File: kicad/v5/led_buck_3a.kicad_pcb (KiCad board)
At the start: 2 copper layers, 44 x 44 mm, 28 parts, among them J1 LED+, J2 LED-, J3 JST_B3B-PH-SM4-TB(LF)(SN), J4 Conn_01x05, Q1 BSC022N04LSATMA, U1 MAX16820ATT, U2 ATtiny1616-M

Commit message: save
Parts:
- added TP1: TestPoint, TestPoint:TestPoint_Pad_1.0x1.0mm, F.Cu at (50.0, 63.8)
- added TP4: TestPoint, TestPoint:TestPoint_Pad_1.0x1.0mm, F.Cu at (48.0, 63.8)
- C1: footprint Capacitor_SMD:C_1210_3225Metric -> Capacitor_SMD:C_0805_2012Metric
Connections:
- U2 pad 15: unconnected-(U2-Pad15) -> Net-(U2-Pad15)
- U2 pad 16: unconnected-(U2-Pad16) -> Net-(U2-Pad16)
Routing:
- net Net-(U2-Pad15): track 0.00 -> 3.03 mm
- net Net-(U2-Pad16): track 0.00 -> 2.82 mm

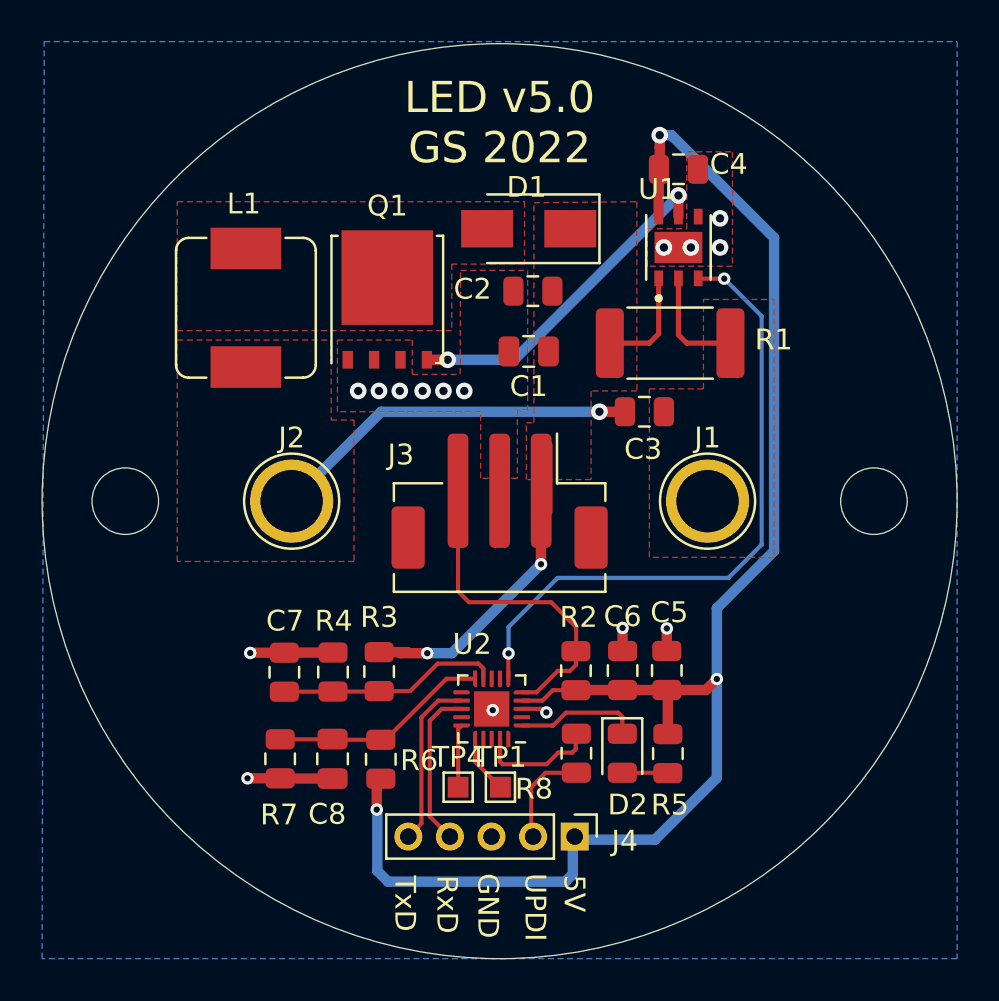
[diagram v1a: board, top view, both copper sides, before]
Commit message: - Neues PCB V5.1 - Ädernungen an den Akkufach 3D Teilen - Firmware überarbeitet
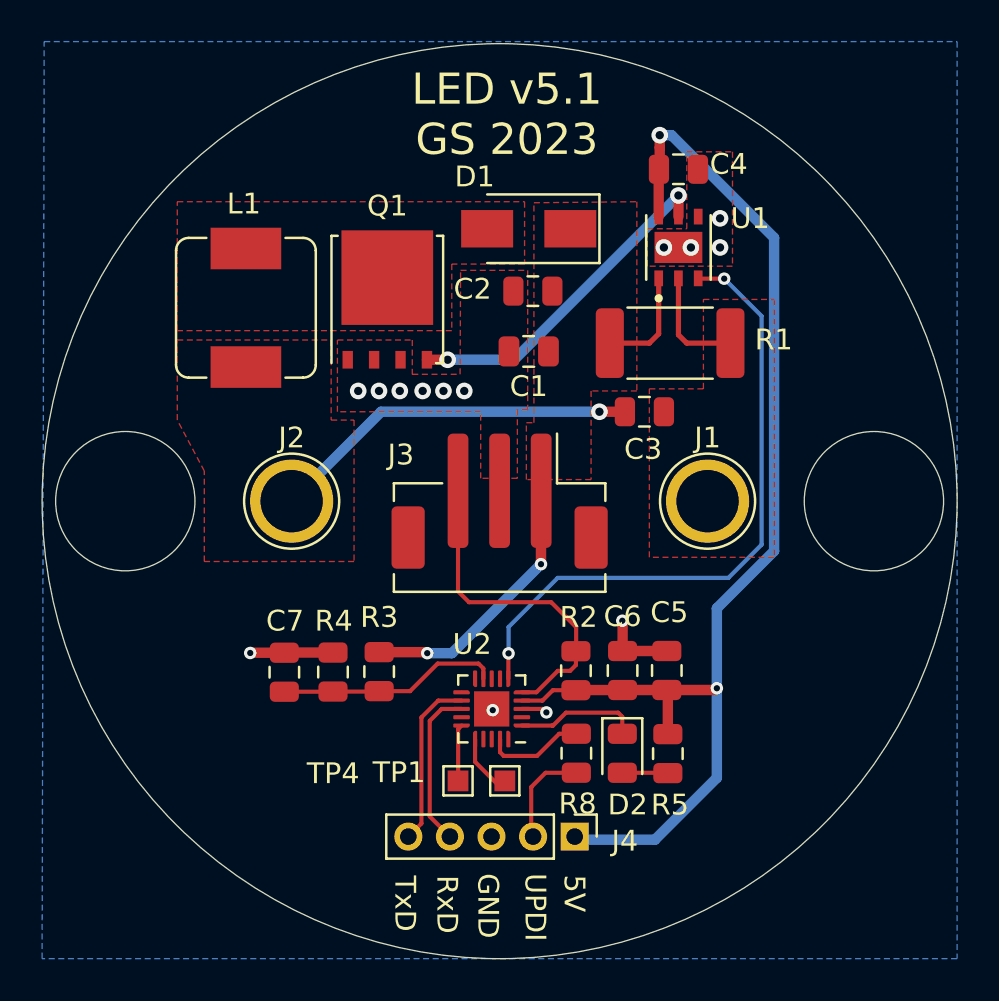
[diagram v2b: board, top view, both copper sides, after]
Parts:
- removed C8: 4n70, Capacitor_SMD:C_0805_2012Metric
- removed R6: 10k0, Resistor_SMD:R_0805_2012Metric
- removed R7: CMFB103F3950FANT, Resistor_SMD:R_0805_2012Metric
- R3: value 82k5 -> 825k
- R4: value 6k81 -> 68k1
- moved TP1 0.37 mm to (50.2, 63.5)
- moved TP4 0.30 mm to (48.0, 63.5)
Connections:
- U2 pad 10: /TMESS -> unconnected-(U2-Pad10)
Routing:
- net +5V: track 74.7 -> 58.5 mm, vias 3 -> 2
- net /TMESS: track 10.7 -> 0.00 mm
- net VCC: track 22.0 -> 18.3 mm
- net GND: track 11.8 -> 8.92 mm, vias 16 -> 14
- net Net-(R8-Pad1): track 5.82 -> 4.79 mm
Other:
- board text added: "LED v5.1 GS 2023"
- board text removed: "LED v5.0 GS 2022"
